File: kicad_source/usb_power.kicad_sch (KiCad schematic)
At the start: 39 parts, among them P1 USB_OTG, Q1 2N7002, Q2 2N7002, Q3 BC847, Q4 BC847, Q5 NTR4171P, SW3 SWITCH_INV, U1 TPS383X, U2 MCP73831, U3 TPS736XX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

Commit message: updated footprint libraries
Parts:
- C1, C2, C3, C4, C5, C6, C7: footprint capacitors:C_0603 -> Capacitor_SMD:C_0603_1608Metric
- C12: footprint capacitors:TantalC_SizeD_EIA-7343_Reflow -> Capacitor_Tantalum_SMD:CP_EIA-7343-31_Kemet-D
- D1, D3, D4: footprint LEDs:LED_0603 -> LED_SMD:LED_0603_1608Metric
- D5: footprint diodes:SOD-123 -> Diode_SMD:D_SOD-123
- F1: footprint fuse_holders_and_fuses:Fuse_SMD1206_Reflow -> Fuse:Fuse_1206_3216Metric
- Q1, Q2, Q3, Q4, Q5, U1: footprint SOT_TO:SOT-23 -> Package_TO_SOT_SMD:SOT-23
- R1, R10, R16, R17, R22, R23, R24, R3, R4, R5, R6, R7, R9: footprint resistors:R_0603 -> Resistor_SMD:R_0603_1608Metric
- U2, U3: footprint SOT_TO:SOT-23-5 -> Package_TO_SOT_SMD:SOT-23-5
- U4: footprint QFN:QFN-28-1EP_5x5mm_Pitch0.5mm -> Package_DFN_QFN:QFN-28-1EP_5x5mm_P0.5mm_EP3.35x3.35mm
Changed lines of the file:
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@@
       (effects (font (size 1.27 1.27)) (justify left))
     )
-    (property "Footprint" "capacitors:TantalC_SizeD_EIA-7343_Reflow" (id 2) (at 156.21 167.64 0)
+    (property "Footprint" "Capacitor_Tantalum_SMD:CP_EIA-7343-31_Kemet-D" (id 2) (at 156.21 167.64 0)
       (effects (font (size 1.27 1.27)) hide)
     )
@@
       (effects (font (size 1.524 1.524)))
     )
-    (property "Footprint" "QFN:QFN-28-1EP_5x5mm_Pitch0.5mm" (id 2) (at 161.29 66.04 0)
+    (property "Footprint" "Package_DFN_QFN:QFN-28-1EP_5x5mm_P0.5mm_EP3.35x3.35mm" (id 2) (at 161.29 66.04 0)
       (effects (font (size 1.524 1.524)) hide)
     )
@@
       (effects (font (size 1.27 1.27)) (justify left))
     )
-    (property "Footprint" "capacitors:C_0603" (id 2) (at 104.14 69.85 0)
+    (property "Footprint" "Capacitor_SMD:C_0603_1608Metric" (id 2) (at 104.14 69.85 0)
       (effects (font (size 1.27 1.27)) hide)
     )
@@
       (effects (font (size 1.27 1.27)) (justify left))
     )
-    (property "Footprint" "capacitors:C_0603" (id 2) (at 110.49 69.85 0)
+    (property "Footprint" "Capacitor_SMD:C_0603_1608Metric" (id 2) (at 110.49 69.85 0)
       (effects (font (size 1.27 1.27)) hide)
     )
@@
       (effects (font (size 1.27 1.27)) (justify left))
     )
-    (property "Footprint" "capacitors:C_0603" (id 2) (at 124.46 72.39 0)
+    (property "Footprint" "Capacitor_SMD:C_0603_1608Metric" (id 2) (at 124.46 72.39 0)
       (effects (font (size 1.27 1.27)) hide)
     )
@@
       (effects (font (size 1.27 1.27)) (justify left))
     )
-    (property "Footprint" "capacitors:C_0603" (id 2) (at 118.11 72.39 0)
+    (property "Footprint" "Capacitor_SMD:C_0603_1608Metric" (id 2) (at 118.11 72.39 0)
       (effects (font (size 1.27 1.27)) hide)
     )
@@
       (effects (font (size 1.27 1.27)) (justify left))
     )
-    (property "Footprint" "resistors:R_0603" (id 2) (at 81.28 67.31 0)
+    (property "Footprint" "Resistor_SMD:R_0603_1608Metric" (id 2) (at 81.28 67.31 0)
       (effects (font (size 1.27 1.27)) hide)
     )
@@
       (effects (font (size 1.27 1.27)) (justify left))
     )
-    (property "Footprint" "resistors:R_0603" (id 2) (at 81.28 74.93 0)
+    (property "Footprint" "Resistor_SMD:R_0603_1608Metric" (id 2) (at 81.28 74.93 0)
       (effects (font (size 1.27 1.27)) hide)
     )
@@
       (effects (font (size 1.27 1.27)) (justify left))
     )
-    (property "Footprint" "resistors:R_0603" (id 2) (at 121.92 53.34 0)
+    (property "Footprint" "Resistor_SMD:R_0603_1608Metric" (id 2) (at 121.92 53.34 0)
       (effects (font (size 1.27 1.27)) hide)
     )
@@
       (effects (font (size 1.27 1.27)) (justify right))
     )
-    (property "Footprint" "LEDs:LED_0603" (id 2) (at 187.96 78.74 90)
+    (property "Footprint" "LED_SMD:LED_0603_1608Metric" (id 2) (at 187.96 78.74 90)
       (effects (font (size 1.27 1.27)) hide)
     )
@@
       (effects (font (size 1.27 1.27)) (justify right))
     )
-    (property "Footprint" "LEDs:LED_0603" (id 2) (at 196.85 78.74 90)
+    (property "Footprint" "LED_SMD:LED_0603_1608Metric" (id 2) (at 196.85 78.74 90)
       (effects (font (size 1.27 1.27)) hide)
     )
@@
       (effects (font (size 1.27 1.27)) (justify left))
     )
-    (property "Footprint" "resistors:R_0603" (id 2) (at 187.96 68.58 0)
+    (property "Footprint" "Resistor_SMD:R_0603_1608Metric" (id 2) (at 187.96 68.58 0)
       (effects (font (size 1.27 1.27)) hide)
     )
@@
       (effects (font (size 1.27 1.27)) (justify left))
     )
-    (property "Footprint" "resistors:R_0603" (id 2) (at 196.85 68.58 0)
+    (property "Footprint" "Resistor_SMD:R_0603_1608Metric" (id 2) (at 196.85 68.58 0)
       (effects (font (size 1.27 1.27)) hide)
     )
@@
       (effects (font (size 1.27 1.27)) (justify left))
     )
-    (property "Footprint" "resistors:R_0603" (id 2) (at 200.66 46.99 0)
+    (property "Footprint" "Resistor_SMD:R_0603_1608Metric" (id 2) (at 200.66 46.99 0)
       (effects (font (size 1.27 1.27)) hide)
     )
@@
       (effects (font (size 1.27 1.27)) (justify left))
     )
-    (property "Footprint" "resistors:R_0603" (id 2) (at 200.66 49.53 0)
+    (property "Footprint" "Resistor_SMD:R_0603_1608Metric" (id 2) (at 200.66 49.53 0)
       (effects (font (size 1.27 1.27)) hide)
     )
@@
       (effects (font (size 1.27 1.27)) (justify left))
     )
-    (property "Footprint" "capacitors:C_0603" (id 2) (at 66.04 175.26 0)
+    (property "Footprint" "Capacitor_SMD:C_0603_1608Metric" (id 2) (at 66.04 175.26 0)
       (effects (font (size 1.27 1.27)) hide)
     )
@@
       (effects (font (size 1.27 1.27)) (justify left))
     )
-    (property "Footprint" "capacitors:C_0603" (id 2) (at 147.32 171.45 0)
+    (property "Footprint" "Capacitor_SMD:C_0603_1608Metric" (id 2) (at 147.32 171.45 0)
       (effects (font (size 1.27 1.27)) hide)
     )
@@
       (effects (font (size 1.27 1.27)) (justify left))
     )
-    (property "Footprint" "resistors:R_0603" (id 2) (at 71.12 129.54 0)
+    (property "Footprint" "Resistor_SMD:R_0603_1608Metric" (id 2) (at 71.12 129.54 0)
       (effects (font (size 1.27 1.27)) hide)
     )
@@
       (effects (font (size 1.27 1.27)) (justify right))
     )
-    (property "Footprint" "LEDs:LED_0603" (id 2) (at 71.12 125.73 90)
+    (property "Footprint" "LED_SMD:LED_0603_1608Metric" (id 2) (at 71.12 125.73 90)
       (effects (font (size 1.27 1.27)) hide)
     )
@@
       (effects (font (size 1.524 1.524)))
     )
-    (property "Footprint" "SOT_TO:SOT-23" (id 2) (at 87.63 166.37 0)
+    (property "Footprint" "Package_TO_SOT_SMD:SOT-23" (id 2) (at 87.63 166.37 0)
       (effects (font (size 1.524 1.524)) hide)
     )
@@
       (effects (font (size 1.524 1.524)))
     )
-    (property "Footprint" "SOT_TO:SOT-23-5" (id 2) (at 124.46 162.56 0)
+    (property "Footprint" "Package_TO_SOT_SMD:SOT-23-5" (id 2) (at 124.46 162.56 0)
       (effects (font (size 1.524 1.524)) hide)
     )
@@
       (effects (font (size 1.524 1.524)))
     )
-    (property "Footprint" "SOT_TO:SOT-23-5" (id 2) (at 95.25 120.65 0)
+    (property "Footprint" "Package_TO_SOT_SMD:SOT-23-5" (id 2) (at 95.25 120.65 0)
       (effects (font (size 1.524 1.524)) hide)
     )
@@
       (effects (font (size 1.27 1.27)) (justify left))
     )
-    (property "Footprint" "capacitors:C_0603" (id 2) (at 64.77 129.54 0)
+    (property "Footprint" "Capacitor_SMD:C_0603_1608Metric" (id 2) (at 64.77 129.54 0)
       (effects (font (size 1.27 1.27)) hide)
     )
@@
       (effects (font (size 1.27 1.27)) (justify left))
     )
-    (property "Footprint" "SOT_TO:SOT-23" (id 2) (at 115.57 135.89 0)
+    (property "Footprint" "Package_TO_SOT_SMD:SOT-23" (id 2) (at 115.57 135.89 0)
       (effects (font (size 1.27 1.27)) hide)
     )
@@
       (effects (font (size 1.27 1.27)) (justify left))
     )
-    (property "Footprint" "SOT_TO:SOT-23" (id 2) (at 143.51 135.89 0)
+    (property "Footprint" "Package_TO_SOT_SMD:SOT-23" (id 2) (at 143.51 135.89 0)
       (effects (font (size 1.27 1.27)) hide)
     )
@@
       (effects (font (size 1.27 1.27)) (justify left))
     )
-    (property "Footprint" "resistors:R_0603" (id 2) (at 118.11 125.73 0)
+    (property "Footprint" "Resistor_SMD:R_0603_1608Metric" (id 2) (at 118.11 125.73 0)
       (effects (font (size 1.27 1.27)) hide)
     )
@@
       (effects (font (size 1.27 1.27)) (justify left))
     )
-    (property "Footprint" "resistors:R_0603" (id 2) (at 146.05 125.73 0)
+    (property "Footprint" "Resistor_SMD:R_0603_1608Metric" (id 2) (at 146.05 125.73 0)
       (effects (font (size 1.27 1.27)) hide)
     )
@@
     (property "Reference" "F1" (id 0) (at 124.46 105.791 0))
     (property "Value" "SF-1206S050" (id 1) (at 124.46 108.1024 0))
-    (property "Footprint" "fuse_holders_and_fuses:Fuse_SMD1206_Reflow" (id 2) (at 124.46 110.49 0)
+    (property "Footprint" "Fuse:Fuse_1206_3216Metric" (id 2) (at 124.46 110.49 0)
       (effects (font (size 1.27 1.27)) hide)
     )
@@
       (effects (font (size 1.27 1.27)) (justify left))
     )
-    (property "Footprint" "SOT_TO:SOT-23" (id 2) (at 253.7714 91.2114 0)
+    (property "Footprint" "Package_TO_SOT_SMD:SOT-23" (id 2) (at 253.7714 91.2114 0)
       (effects (font (size 1.27 1.27)) (justify left) hide)
     )
@@
       (effects (font (size 1.27 1.27)) (justify left))
     )
-    (property "Footprint" "resistors:R_0603" (id 2) (at 232.41 88.9 0)
+    (property "Footprint" "Resistor_SMD:R_0603_1608Metric" (id 2) (at 232.41 88.9 0)
       (effects (font (size 1.27 1.27)) hide)
     )
@@
       (effects (font (size 1.27 1.27)) (justify left))
     )
-    (property "Footprint" "SOT_TO:SOT-23" (id 2) (at 254 127 0)
+    (property "Footprint" "Package_TO_SOT_SMD:SOT-23" (id 2) (at 254 127 0)
       (effects (font (size 1.27 1.27)) hide)
     )
@@
       (effects (font (size 1.27 1.27)) (justify left))
     )
-    (property "Footprint" "resistors:R_0603" (id 2) (at 232.41 129.54 0)
+    (property "Footprint" "Resistor_SMD:R_0603_1608Metric" (id 2) (at 232.41 129.54 0)
       (effects (font (size 1.27 1.27)) hide)
     )
@@
       (effects (font (size 1.27 1.27)) (justify left))
     )
-    (property "Footprint" "SOT_TO:SOT-23" (id 2) (at 50.8 95.25 0)
+    (property "Footprint" "Package_TO_SOT_SMD:SOT-23" (id 2) (at 50.8 95.25 0)
       (effects (font (size 1.27 1.27)) hide)
     )
@@
       (effects (font (size 1.27 1.27)) (justify left))
     )
-    (property "Footprint" "resistors:R_0603" (id 2) (at 29.21 97.79 0)
+    (property "Footprint" "Resistor_SMD:R_0603_1608Metric" (id 2) (at 29.21 97.79 0)
       (effects (font (size 1.27 1.27)) hide)
     )
@@
     (property "Reference" "D5" (id 0) (at 34.29 105.283 0))
     (property "Value" "MBR120" (id 1) (at 34.29 107.5944 0))
-    (property "Footprint" "diodes:SOD-123" (id 2) (at 34.29 110.49 90)
-      (effects (font (size 1.27 1.27)) hide)
-    )
+    (property "Footprint" "Diode_SMD:D_SOD-123" (id 2) (at 34.29 110.49 90)
+      (effects (font (size 1.27 1.27)) hide)
+    )

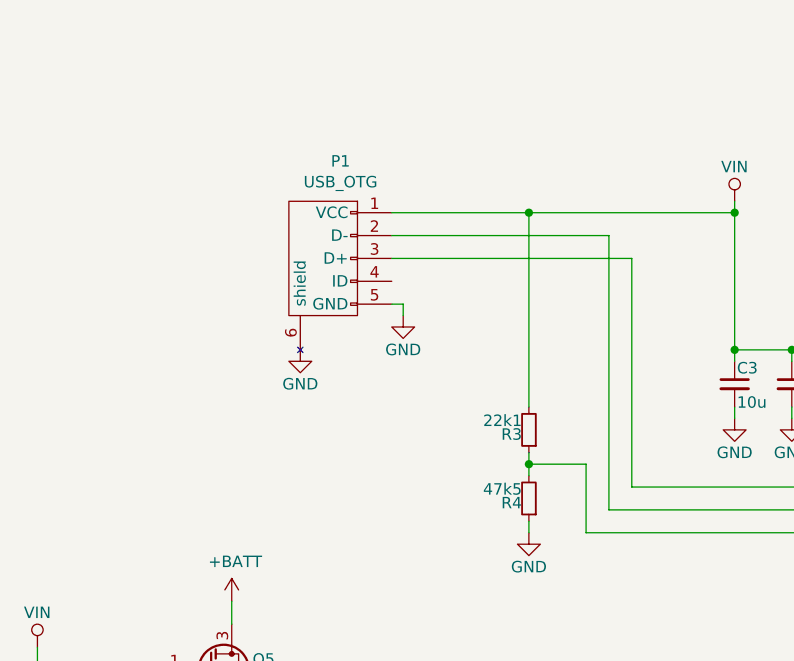
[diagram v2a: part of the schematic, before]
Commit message: added usb c connector
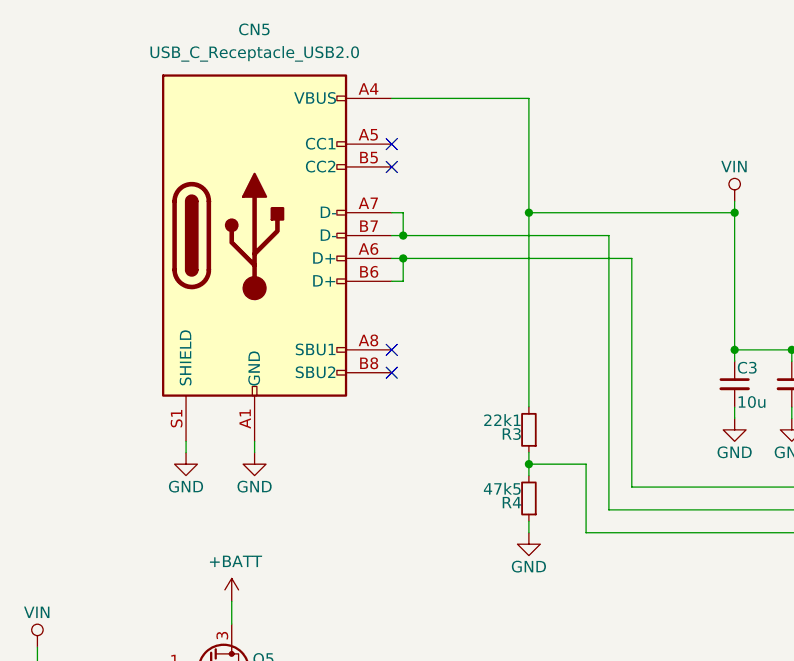
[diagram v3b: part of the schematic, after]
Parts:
- removed P1: USB_OTG, CON_wuerth:WE_629105136821, symbol sensornator-rescue:USB_OTG-mechanical-connectors
- added CN5: USB_C_Receptacle_USB2.0, Connector_USB:USB_C_Receptacle_Amphenol_12401610E4-2A, symbol Connector:USB_C_Receptacle_USB2.0
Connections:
- net GND: now also CN5.A1 (GND), CN5.A12 (GND), CN5.B1 (GND), CN5.B12 (GND), CN5.S1 (SHIELD)
- net VIN: now also CN5.A4 (VBUS), CN5.A9 (VBUS), CN5.B4 (VBUS), CN5.B9 (VBUS)
- net at U4.5 (D-): now also CN5.A7 (D-), CN5.B7 (D-)
- net at U4.4 (D+): now also CN5.A6 (D+), CN5.B6 (D+)
- no-connect marks 15 -> 19
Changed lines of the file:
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@@
   (junction (at 104.14 62.23) (diameter 0) (color 0 0 0 0)
   )
+  (junction (at 81.28 46.99) (diameter 0) (color 0 0 0 0)
+  )
   (junction (at 110.49 62.23) (diameter 0) (color 0 0 0 0)
   )
@@
   (junction (at 124.46 64.77) (diameter 0) (color 0 0 0 0)
   )
+  (junction (at 67.31 49.53) (diameter 0) (color 0 0 0 0)
+  )
+  (junction (at 67.31 52.07) (diameter 0) (color 0 0 0 0)
+  )
   (junction (at 220.98 137.16) (diameter 0) (color 0 0 0 0)
   )
@@
   )
   (junction (at 139.7 85.09) (diameter 0) (color 0 0 0 0)
-  )
-  (junction (at 81.28 46.99) (diameter 0) (color 0 0 0 0)
   )
   (junction (at 81.28 74.93) (diameter 0) (color 0 0 0 0)
@@
   (no_connect (at 140.97 46.99))
   (no_connect (at 140.97 167.64))
+  (no_connect (at 66.04 39.37))
+  (no_connect (at 66.04 41.91))
+  (no_connect (at 66.04 62.23))
+  (no_connect (at 66.04 64.77))
   (no_connect (at 140.97 52.07))
   (no_connect (at 180.34 72.39))
@@
     (stroke (width 0) (type default) (color 0 0 0 0))
   )
-  (wire (pts (xy 66.04 49.53) (xy 90.17 49.53))
+  (wire (pts (xy 66.04 49.53) (xy 67.31 49.53))
     (stroke (width 0) (type default) (color 0 0 0 0))
   )
@@
     (stroke (width 0) (type default) (color 0 0 0 0))
   )
+  (wire (pts (xy 66.04 34.29) (xy 81.28 34.29))
+    (stroke (width 0) (type default) (color 0 0 0 0))
+  )
   (wire (pts (xy 64.77 121.92) (xy 64.77 120.65))
     (stroke (width 0) (type default) (color 0 0 0 0))
@@
     (stroke (width 0) (type default) (color 0 0 0 0))
   )
+  (wire (pts (xy 66.04 54.61) (xy 67.31 54.61))
+    (stroke (width 0) (type default) (color 0 0 0 0))
+  )
   (wire (pts (xy 118.11 144.78) (xy 118.11 143.51))
     (stroke (width 0) (type default) (color 0 0 0 0))
@@
     (stroke (width 0) (type default) (color 0 0 0 0))
   )
+  (wire (pts (xy 81.28 34.29) (xy 81.28 46.99))
+    (stroke (width 0) (type default) (color 0 0 0 0))
+  )
   (wire (pts (xy 118.11 64.77) (xy 124.46 64.77))
     (stroke (width 0) (type default) (color 0 0 0 0))
@@
     (stroke (width 0) (type default) (color 0 0 0 0))
   )
-  (wire (pts (xy 92.71 52.07) (xy 66.04 52.07))
+  (wire (pts (xy 92.71 52.07) (xy 67.31 52.07))
     (stroke (width 0) (type default) (color 0 0 0 0))
   )
@@
     (stroke (width 0) (type default) (color 0 0 0 0))
   )
-  (wire (pts (xy 66.04 46.99) (xy 81.28 46.99))
-    (stroke (width 0) (type default) (color 0 0 0 0))
-  )
   (wire (pts (xy 104.14 46.99) (xy 104.14 62.23))
     (stroke (width 0) (type default) (color 0 0 0 0))
@@
     (stroke (width 0) (type default) (color 0 0 0 0))
   )
+  (wire (pts (xy 67.31 49.53) (xy 90.17 49.53))
+    (stroke (width 0) (type default) (color 0 0 0 0))
+  )
   (wire (pts (xy 48.26 90.17) (xy 48.26 92.71))
     (stroke (width 0) (type default) (color 0 0 0 0))
@@
     (stroke (width 0) (type default) (color 0 0 0 0))
   )
+  (wire (pts (xy 67.31 52.07) (xy 66.04 52.07))
+    (stroke (width 0) (type default) (color 0 0 0 0))
+  )
   (wire (pts (xy 66.04 166.37) (xy 66.04 167.64))
     (stroke (width 0) (type default) (color 0 0 0 0))
@@
     (stroke (width 0) (type default) (color 0 0 0 0))
   )
+  (wire (pts (xy 67.31 46.99) (xy 67.31 49.53))
+    (stroke (width 0) (type default) (color 0 0 0 0))
+  )
   (wire (pts (xy 90.17 80.01) (xy 137.16 80.01))
     (stroke (width 0) (type default) (color 0 0 0 0))
@@
     (stroke (width 0) (type default) (color 0 0 0 0))
   )
+  (wire (pts (xy 66.04 46.99) (xy 67.31 46.99))
+    (stroke (width 0) (type default) (color 0 0 0 0))
+  )
   (wire (pts (xy 130.81 69.85) (xy 140.97 69.85))
     (stroke (width 0) (type default) (color 0 0 0 0))
@@
     (stroke (width 0) (type default) (color 0 0 0 0))
   )
-  (wire (pts (xy 67.31 57.15) (xy 67.31 58.42))
-    (stroke (width 0) (type default) (color 0 0 0 0))
-  )
   (wire (pts (xy 121.92 110.49) (xy 116.84 110.49))
     (stroke (width 0) (type default) (color 0 0 0 0))
@@
     (stroke (width 0) (type default) (color 0 0 0 0))
   )
+  (wire (pts (xy 67.31 54.61) (xy 67.31 52.07))
+    (stroke (width 0) (type default) (color 0 0 0 0))
+  )
   (wire (pts (xy 196.85 81.28) (xy 196.85 85.09))
     (stroke (width 0) (type default) (color 0 0 0 0))
@@
     (stroke (width 0) (type default) (color 0 0 0 0))
   )
-  (wire (pts (xy 66.04 57.15) (xy 67.31 57.15))
-    (stroke (width 0) (type default) (color 0 0 0 0))
-  )
   (wire (pts (xy 107.95 163.83) (xy 106.68 163.83))
     (stroke (width 0) (type default) (color 0 0 0 0))
@@
     (stroke (width 0) (type default) (color 0 0 0 0))
   )
+  (wire (pts (xy 50.8 72.39) (xy 50.8 73.66))
+    (stroke (width 0) (type default) (color 0 0 0 0))
+  )
   (wire (pts (xy 30.48 97.79) (xy 26.67 97.79))
     (stroke (width 0) (type default) (color 0 0 0 0))
@@
   )
   (wire (pts (xy 140.97 82.55) (xy 139.7 82.55))
+    (stroke (width 0) (type default) (color 0 0 0 0))
+  )
+  (wire (pts (xy 43.18 72.39) (xy 43.18 73.66))
     (stroke (width 0) (type default) (color 0 0 0 0))
   )
@@
     (pin "3")
   )
-  (symbol (lib_id "sensornator-rescue:USB_OTG-mechanical-connectors") (at 58.42 52.07 90) (mirror x) (unit 1)
-    (in_bom yes) (on_board yes)
-    (property "Reference" "P1" (id 0) (at 60.3504 41.275 90))
-    (property "Value" "USB_OTG" (id 1) (at 60.3504 43.5864 90))
-    (property "Footprint" "CON_wuerth:WE_629105136821" (id 2) (at 60.96 50.8 90)
-      (effects (font (size 1.27 1.27)) hide)
-    )
-    (property "Datasheet" "" (id 3) (at 60.96 50.8 90))
-    (pin "1")
-    (pin "2")
-    (pin "3")
-    (pin "4")
-    (pin "5")
-    (pin "6")
-  )
-  (symbol (lib_id "power:GND") (at 55.88 62.23 0) (unit 1)
-    (in_bom yes) (on_board yes)
-    (property "Reference" "#PWR0105" (id 0) (at 55.88 68.58 0)
-      (effects (font (size 1.27 1.27)) hide)
-    )
-    (property "Value" "GND" (id 1) (at 55.88 66.04 0))
-    (property "Footprint" "" (id 2) (at 55.88 62.23 0))
-    (property "Datasheet" "" (id 3) (at 55.88 62.23 0))
-    (pin "1")
-  )
-  (symbol (lib_id "power:GND") (at 67.31 58.42 0) (unit 1)
-    (in_bom yes) (on_board yes)
-    (property "Reference" "#PWR0106" (id 0) (at 67.31 64.77 0)
-      (effects (font (size 1.27 1.27)) hide)
-    )
-    (property "Value" "GND" (id 1) (at 67.31 62.23 0))
-    (property "Footprint" "" (id 2) (at 67.31 58.42 0))
-    (property "Datasheet" "" (id 3) (at 67.31 58.42 0))
+  (symbol (lib_id "power:GND") (at 43.18 73.66 0) (unit 1)
+    (in_bom yes) (on_board yes)
+    (property "Reference" "#PWR0105" (id 0) (at 43.18 80.01 0)
+      (effects (font (size 1.27 1.27)) hide)
+    )
+    (property "Value" "GND" (id 1) (at 43.18 77.47 0))
+    (property "Footprint" "" (id 2) (at 43.18 73.66 0))
+    (property "Datasheet" "" (id 3) (at 43.18 73.66 0))
+    (pin "1")
+  )
+  (symbol (lib_id "power:GND") (at 50.8 73.66 0) (unit 1)
+    (in_bom yes) (on_board yes)
+    (property "Reference" "#PWR0106" (id 0) (at 50.8 80.01 0)
+      (effects (font (size 1.27 1.27)) hide)
+    )
+    (property "Value" "GND" (id 1) (at 50.8 77.47 0))
+    (property "Footprint" "" (id 2) (at 50.8 73.66 0))
+    (property "Datasheet" "" (id 3) (at 50.8 73.66 0))
     (pin "1")
   )
@@
     (pin "2")
   )
+  (symbol (lib_id "Connector:USB_C_Receptacle_USB2.0") (at 50.8 49.53 0) (unit 1)
+    (in_bom yes) (on_board yes) (fields_autoplaced)
+    (property "Reference" "CN5" (id 0) (at 50.8 26.67 0))
+    (property "Value" "USB_C_Receptacle_USB2.0" (id 1) (at 50.8 29.21 0))
+    (property "Footprint" "Connector_USB:USB_C_Receptacle_Amphenol_12401610E4-2A" (id 2) (at 54.61 49.53 0)
+      (effects (font (size 1.27 1.27)) hide)
+    )
+    (property "Datasheet" "https://www.usb.org/sites/default/files/documents/usb_type-c.zip" (id 3) (at 54.61 49.53 0)
+      (effects (font (size 1.27 1.27)) hide)
+    )
+    (pin "A1")
+    (pin "A12")
+    (pin "A4")
+    (pin "A5")
+    (pin "A6")
+    (pin "A7")
+    (pin "A8")
+    (pin "A9")
+    (pin "B1")
+    (pin "B12")
+    (pin "B4")
+    (pin "B5")
+    (pin "B6")
+    (pin "B7")
+    (pin "B8")
+    (pin "B9")
+    (pin "S1")
+  )
   (symbol (lib_id "Device:R_Small") (at 251.46 118.11 180) (unit 1)
